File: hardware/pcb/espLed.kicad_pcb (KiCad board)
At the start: 2 copper layers, 23 parts, among them J1 led_strip, J2 flashing, J3 power, Q1 IRF9310TRPBF, Q2 AO3400A, Q3 AO3400A, Q4 AO3400A, SW1 reset, SW2 flash, U1 AMS1117-3.3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

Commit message: connect GNDs of two transistors and make strip's 12v trace thicker
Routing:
- net GND: track 124.1 -> 186.6 mm
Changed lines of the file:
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@@
     (thickness 1.6)
     (drawings 0)
-    (tracks 175)
+    (tracks 191)
     (zones 0)
     (modules 23)
@@
   )
   (setup
-    (last_trace_width 0.6)
+    (last_trace_width 0.4)
     (user_trace_width 0.4)
     (user_trace_width 0.6)
+    (user_trace_width 0.8)
     (trace_clearance 0.3)
     (zone_clearance 0.508)
@@
   (segment (start 182.555 111.252) (end 191.262 111.252) (width 0.4) (layer B.Cu) (net 1))
   (segment (start 176.262 117.545) (end 182.555 111.252) (width 0.4) (layer B.Cu) (net 1))
-  (segment (start 190.246 116.586) (end 191.262 117.602) (width 0.4) (layer F.Cu) (net 1))
-  (segment (start 184.658 117.475) (end 185.547 116.586) (width 0.4) (layer F.Cu) (net 1))
-  (segment (start 184.658 131.064) (end 184.658 117.475) (width 0.4) (layer F.Cu) (net 1))
-  (segment (start 185.814 132.22) (end 184.658 131.064) (width 0.4) (layer F.Cu) (net 1))
-  (segment (start 186.28 132.22) (end 185.814 132.22) (width 0.4) (layer F.Cu) (net 1))
   (segment (start 184.702001 136.906) (end 169.2425 136.906) (width 0.4) (layer F.Cu) (net 1))
   (segment (start 169.2425 136.906) (end 168.148 135.8115) (width 0.4) (layer F.Cu) (net 1))
   (segment (start 186.28 135.328001) (end 184.702001 136.906) (width 0.4) (layer F.Cu) (net 1))
-  (segment (start 192.024 117.602) (end 191.262 117.602) (width 0.4) (layer B.Cu) (net 1))
-  (segment (start 193.04 140.208) (end 193.04 118.618) (width 0.4) (layer B.Cu) (net 1))
+  (segment (start 192.532 117.602) (end 191.262 117.602) (width 0.4) (layer B.Cu) (net 1))
+  (segment (start 193.04 118.11) (end 192.532 117.602) (width 0.4) (layer B.Cu) (net 1))
+  (segment (start 193.04 140.208) (end 193.04 118.11) (width 0.4) (layer B.Cu) (net 1))
   (segment (start 192.278 140.97) (end 193.04 140.208) (width 0.4) (layer B.Cu) (net 1))
-  (segment (start 193.04 118.618) (end 192.024 117.602) (width 0.4) (layer B.Cu) (net 1))
   (segment (start 188.976 140.97) (end 192.278 140.97) (width 0.4) (layer B.Cu) (net 1))
   (segment (start 188.468 140.462) (end 188.976 140.97) (width 0.4) (layer B.Cu) (net 1))
   (segment (start 188.468 138.938) (end 188.468 140.462) (width 0.4) (layer B.Cu) (net 1))
-  (segment (start 191.262 111.252) (end 185.928 116.586) (width 0.4) (layer F.Cu) (net 1))
-  (segment (start 185.928 116.586) (end 190.246 116.586) (width 0.4) (layer F.Cu) (net 1))
-  (segment (start 185.547 116.586) (end 185.928 116.586) (width 0.4) (layer F.Cu) (net 1))
+  (segment (start 187.198 120.65) (end 190.246 117.602) (width 0.8) (layer B.Cu) (net 1))
+  (segment (start 187.198 127.508) (end 187.198 120.65) (width 0.8) (layer B.Cu) (net 1))
+  (segment (start 190.246 117.602) (end 191.262 117.602) (width 0.6) (layer B.Cu) (net 1))
+  (segment (start 182.438 133.366) (end 182.438 132.268) (width 0.6) (layer B.Cu) (net 1))
+  (segment (start 185.293 129.413) (end 187.198 127.508) (width 0.8) (layer B.Cu) (net 1))
+  (segment (start 182.438 132.268) (end 185.293 129.413) (width 0.6) (layer B.Cu) (net 1))
+  (segment (start 173.99 130.048) (end 184.658 130.048) (width 0.6) (layer B.Cu) (net 1))
+  (segment (start 170.942 127) (end 173.99 130.048) (width 0.6) (layer B.Cu) (net 1))
+  (segment (start 164.846 127) (end 170.942 127) (width 0.6) (layer B.Cu) (net 1))
+  (segment (start 184.658 130.048) (end 185.293 129.413) (width 0.8) (layer B.Cu) (net 1))
+  (segment (start 163.068 128.778) (end 164.846 127) (width 0.6) (layer B.Cu) (net 1))
+  (segment (start 163.068 133.096) (end 163.068 128.778) (width 0.6) (layer B.Cu) (net 1))
+  (segment (start 165.862 135.89) (end 163.068 133.096) (width 0.6) (layer B.Cu) (net 1))
+  (segment (start 169.926 135.89) (end 165.862 135.89) (width 0.6) (layer B.Cu) (net 1))
+  (segment (start 172.45 133.366) (end 169.926 135.89) (width 0.6) (layer B.Cu) (net 1))
+  (segment (start 174.818 133.366) (end 172.45 133.366) (width 0.6) (layer B.Cu) (net 1))
+  (segment (start 190.246 117.602) (end 191.262 117.602) (width 0.8) (layer F.Cu) (net 1))
+  (segment (start 189.23 112.081919) (end 189.23 116.586) (width 0.8) (layer F.Cu) (net 1))
+  (segment (start 189.23 116.586) (end 190.246 117.602) (width 0.8) (layer F.Cu) (net 1))
+  (segment (start 190.059919 111.252) (end 189.23 112.081919) (width 0.8) (layer F.Cu) (net 1))
+  (segment (start 191.262 111.252) (end 190.059919 111.252) (width 0.8) (layer F.Cu) (net 1))
+  (segment (start 184.658 131.064) (end 184.658 117.348) (width 0.4) (layer F.Cu) (net 1))
+  (segment (start 185.814 132.22) (end 184.658 131.064) (width 0.4) (layer F.Cu) (net 1))
+  (segment (start 186.28 132.22) (end 185.814 132.22) (width 0.4) (layer F.Cu) (net 1))
+  (segment (start 185.42 116.586) (end 189.23 116.586) (width 0.4) (layer F.Cu) (net 1))
+  (segment (start 184.658 117.348) (end 185.42 116.586) (width 0.4) (layer F.Cu) (net 1))
   (segment (start 176.462 123.7) (end 176.512 123.65) (width 0.4) (layer B.Cu) (net 2))
   (segment (start 174.0995 123.7) (end 176.462 123.7) (width 0.4) (layer B.Cu) (net 2))
@@
   (segment (start 183.642 113.792) (end 181.562 115.872) (width 0.4) (layer B.Cu) (net 9))
   (segment (start 191.262 113.792) (end 183.642 113.792) (width 0.4) (layer B.Cu) (net 9))
-  (segment (start 175.514 141.732) (end 174.498 140.716) (width 0.6) (layer B.Cu) (net 9))
-  (segment (start 187.99801 141.77001) (end 187.96 141.732) (width 0.6) (layer B.Cu) (net 9))
-  (segment (start 192.805682 141.77001) (end 187.99801 141.77001) (width 0.6) (layer B.Cu) (net 9))
-  (segment (start 194.818 139.757692) (end 192.805682 141.77001) (width 0.6) (layer B.Cu) (net 9))
-  (segment (start 194.818 115.316) (end 194.818 139.757692) (width 0.6) (layer B.Cu) (net 9))
-  (segment (start 187.96 141.732) (end 175.514 141.732) (width 0.6) (layer B.Cu) (net 9))
-  (segment (start 193.294 113.792) (end 194.818 115.316) (width 0.6) (layer B.Cu) (net 9))
-  (segment (start 174.498 140.716) (end 174.498 138.938) (width 0.6) (layer B.Cu) (net 9))
-  (segment (start 191.262 113.792) (end 193.294 113.792) (width 0.6) (layer B.Cu) (net 9))
+  (segment (start 174.498 140.716) (end 174.498 138.938) (width 0.8) (layer B.Cu) (net 9))
+  (segment (start 175.768 141.986) (end 174.498 140.716) (width 0.8) (layer B.Cu) (net 9))
+  (segment (start 193.04 141.986) (end 175.768 141.986) (width 0.8) (layer B.Cu) (net 9))
+  (segment (start 194.056 140.97) (end 193.04 141.986) (width 0.8) (layer B.Cu) (net 9))
+  (segment (start 194.056 114.554) (end 194.056 140.97) (width 0.8) (layer B.Cu) (net 9))
+  (segment (start 193.294 113.792) (end 194.056 114.554) (width 0.8) (layer B.Cu) (net 9))
+  (segment (start 191.262 113.792) (end 193.294 113.792) (width 0.8) (layer B.Cu) (net 9))
   (via (at 191.008 126.492) (size 1.6) (drill 1) (layers F.Cu B.Cu) (net 10))
   (segment (start 192.1995 127.6835) (end 191.008 126.492) (width 0.4) (layer F.Cu) (net 10))

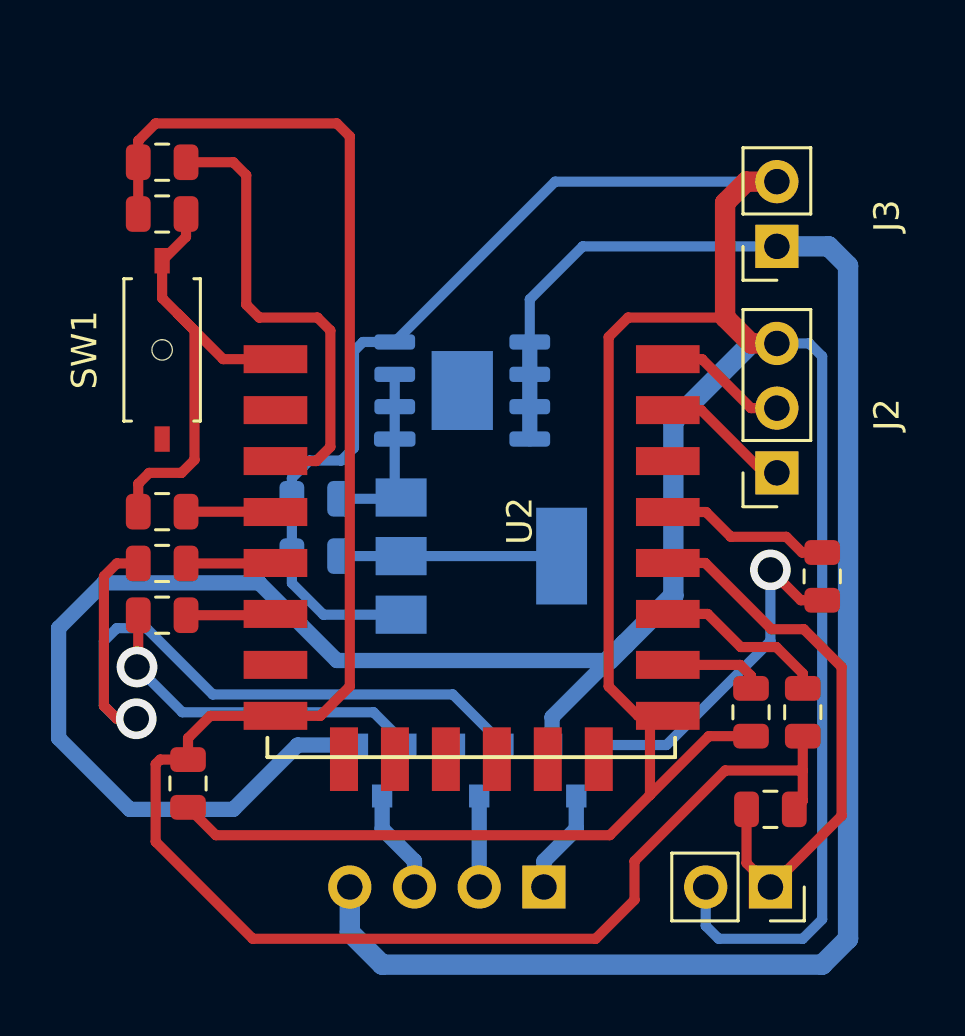
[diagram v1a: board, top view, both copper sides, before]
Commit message: connect GND of the remaining transistor and make 12V traces thicker
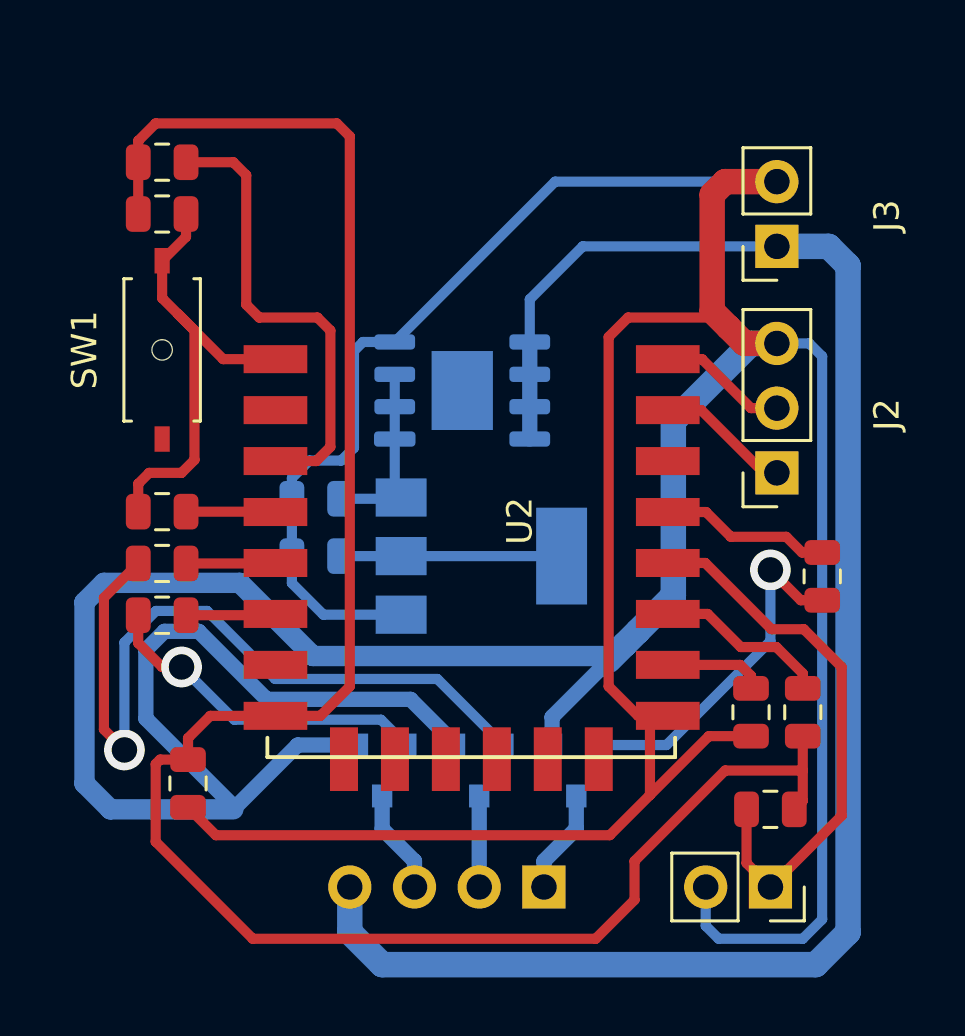
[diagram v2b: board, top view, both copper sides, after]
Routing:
- net GND: track 186.6 -> 211.5 mm
- net Net-(Q4-Pad2): track 13.9 -> 13.3 mm

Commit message: connect 3v3 of the regulator to ESP and connect GND of the "reset" btn
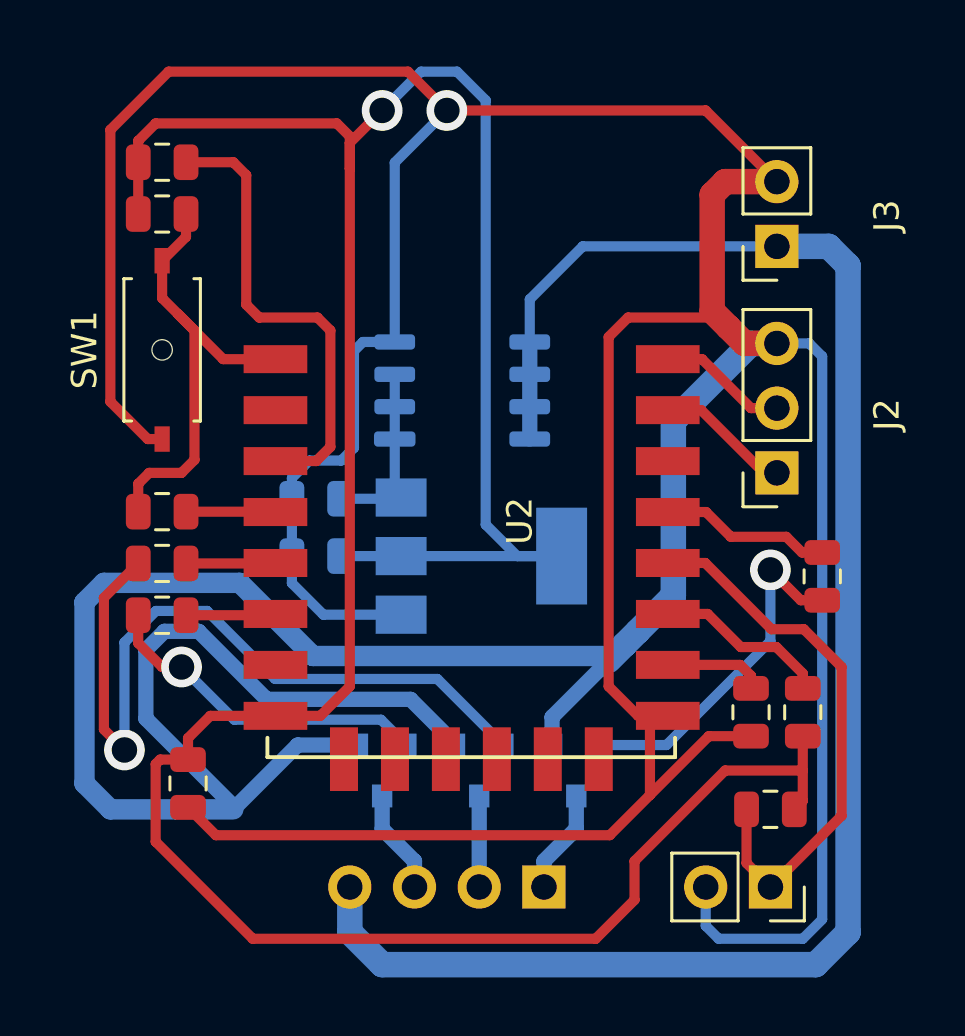
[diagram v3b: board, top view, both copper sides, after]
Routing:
- net GND: track 211.5 -> 246.0 mm, vias 0 -> 1
- net +3V3: track 88.6 -> 116.7 mm, vias 0 -> 1
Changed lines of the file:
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@@
     (thickness 1.6)
     (drawings 0)
-    (tracks 202)
+    (tracks 221)
     (zones 0)
     (modules 23)
@@
     (fp_line (start 3.7 -2.7) (end 3.7 2.7) (layer B.CrtYd) (width 0.05))
     (fp_line (start 3.7 2.7) (end -3.7 2.7) (layer B.CrtYd) (width 0.05))
-    (fp_text user %R (at 0 0 180) (layer B.Fab)
-      (effects (font (size 0.98 0.98) (thickness 0.15)) (justify mirror))
-    )
     (pad 3 smd roundrect (at -2.65 1.905) (size 1.63 0.6) (layers B.Cu B.Paste B.Mask) (roundrect_rratio 0.25)
       (net 2 +12V))
@@
     (pad 1 smd roundrect (at 2.65 1.905) (size 1.6 0.6) (layers B.Cu B.Paste B.Mask) (roundrect_rratio 0.25)
       (net 9 /12v_in))
-    (pad 9 smd rect (at 0 0) (size 2.41 3.1) (layers B.Cu B.Mask))
-    (pad "" smd roundrect (at -0.6 0.775) (size 0.97 1.25) (layers B.Paste) (roundrect_rratio 0.25))
-    (pad "" smd roundrect (at -0.6 -0.775) (size 0.97 1.25) (layers B.Paste) (roundrect_rratio 0.25))
-    (pad "" smd roundrect (at 0.6 0.775) (size 0.97 1.25) (layers B.Paste) (roundrect_rratio 0.25))
-    (pad "" smd roundrect (at 0.6 -0.775) (size 0.97 1.25) (layers B.Paste) (roundrect_rratio 0.25))
     (model ${KISYS3DMOD}/Package_SO.3dshapes/HSOP-8-1EP_3.9x4.9mm_P1.27mm_EP2.41x3.1mm.wrl
       (at (xyz 0 0 0))
@@
   (segment (start 188.590501 133.0175) (end 186.28 135.328001) (width 0.4) (layer F.Cu) (net 1))
   (segment (start 190.246 133.0175) (end 188.590501 133.0175) (width 0.4) (layer F.Cu) (net 1))
-  (segment (start 182.555 111.252) (end 191.262 111.252) (width 0.4) (layer B.Cu) (net 1))
-  (segment (start 176.262 117.545) (end 182.555 111.252) (width 0.4) (layer B.Cu) (net 1))
   (segment (start 184.702001 136.906) (end 169.2425 136.906) (width 0.4) (layer F.Cu) (net 1))
   (segment (start 169.2425 136.906) (end 168.148 135.8115) (width 0.4) (layer F.Cu) (net 1))
@@
   (segment (start 189.357 116.967) (end 188.722 116.332) (width 1) (layer F.Cu) (net 1))
   (segment (start 189.992 117.602) (end 189.357 116.967) (width 1) (layer F.Cu) (net 1))
+  (via (at 178.308 108.458) (size 1.6) (drill 1) (layers F.Cu B.Cu) (net 1))
+  (segment (start 176.262 117.545) (end 176.262 110.504) (width 0.4) (layer B.Cu) (net 1))
+  (segment (start 176.262 110.504) (end 178.308 108.458) (width 0.4) (layer B.Cu) (net 1))
+  (segment (start 191.262 111.252) (end 188.468 108.458) (width 0.4) (layer F.Cu) (net 1))
+  (segment (start 188.468 108.458) (end 178.308 108.458) (width 0.4) (layer F.Cu) (net 1))
+  (segment (start 166.568 121.356) (end 167.132 121.356) (width 0.4) (layer F.Cu) (net 1))
+  (segment (start 165.1 119.888) (end 166.568 121.356) (width 0.4) (layer F.Cu) (net 1))
+  (segment (start 165.1 109.22) (end 165.1 119.888) (width 0.4) (layer F.Cu) (net 1))
+  (segment (start 167.386 106.934) (end 165.1 109.22) (width 0.4) (layer F.Cu) (net 1))
+  (segment (start 176.784 106.934) (end 167.386 106.934) (width 0.4) (layer F.Cu) (net 1))
+  (segment (start 178.308 108.458) (end 176.784 106.934) (width 0.4) (layer F.Cu) (net 1))
   (segment (start 176.462 123.7) (end 176.512 123.65) (width 0.4) (layer B.Cu) (net 2))
   (segment (start 174.0995 123.7) (end 176.462 123.7) (width 0.4) (layer B.Cu) (net 2))
@@
   (segment (start 166.878 134.112) (end 167.0535 133.9365) (width 0.4) (layer F.Cu) (net 3))
   (segment (start 173.342 132.22) (end 172.28 132.22) (width 0.4) (layer F.Cu) (net 3))
-  (segment (start 174.498 109.474) (end 174.498 131.064) (width 0.4) (layer F.Cu) (net 3))
   (segment (start 173.99 108.966) (end 174.498 109.474) (width 0.4) (layer F.Cu) (net 3))
   (segment (start 174.498 131.064) (end 173.342 132.22) (width 0.4) (layer F.Cu) (net 3))
@@
   (segment (start 166.1945 109.6495) (end 166.878 108.966) (width 0.4) (layer F.Cu) (net 3))
   (segment (start 166.1945 110.49) (end 166.1945 109.6495) (width 0.4) (layer F.Cu) (net 3))
+  (segment (start 182.812 125.95) (end 181.068 125.95) (width 0.4) (layer B.Cu) (net 3))
+  (segment (start 181.068 125.95) (end 179.832 124.714) (width 0.4) (layer B.Cu) (net 3))
+  (segment (start 179.832 108.057998) (end 178.708002 106.934) (width 0.4) (layer B.Cu) (net 3))
+  (segment (start 179.832 124.714) (end 179.832 108.057998) (width 0.4) (layer B.Cu) (net 3))
+  (via (at 175.768 108.458) (size 1.6) (drill 1) (layers F.Cu B.Cu) (net 3))
+  (segment (start 177.292 106.934) (end 175.768 108.458) (width 0.4) (layer B.Cu) (net 3))
+  (segment (start 178.708002 106.934) (end 177.292 106.934) (width 0.4) (layer B.Cu) (net 3))
+  (segment (start 174.498 109.728) (end 174.498 110.744) (width 0.4) (layer F.Cu) (net 3))
+  (segment (start 175.768 108.458) (end 174.498 109.728) (width 0.4) (layer F.Cu) (net 3))
+  (segment (start 174.498 110.744) (end 174.498 131.064) (width 0.4) (layer F.Cu) (net 3))
+  (segment (start 174.498 109.474) (end 174.498 110.744) (width 0.4) (layer F.Cu) (net 3))
   (segment (start 175.768 136.652) (end 177.038 137.922) (width 0.6) (layer B.Cu) (net 4))
   (segment (start 177.038 137.922) (end 177.038 138.938) (width 0.6) (layer B.Cu) (net 4))
@@
   (segment (start 186.28 120.22) (end 188.292 120.22) (width 0.4) (layer F.Cu) (net 8))
   (segment (start 181.562 117.545) (end 181.562 121.355) (width 0.6) (layer B.Cu) (net 9))
-  (segment (start 181.562 115.872) (end 181.562 117.545) (width 0.4) (layer B.Cu) (net 9))
-  (segment (start 183.642 113.792) (end 181.562 115.872) (width 0.4) (layer B.Cu) (net 9))
-  (segment (start 191.262 113.792) (end 183.642 113.792) (width 0.4) (layer B.Cu) (net 9))
   (segment (start 175.768 141.986) (end 174.498 140.716) (width 1) (layer B.Cu) (net 9))
   (segment (start 192.786 141.986) (end 175.768 141.986) (width 1) (layer B.Cu) (net 9))
@@
   (segment (start 193.294 113.792) (end 194.056 114.554) (width 1) (layer B.Cu) (net 9))
   (segment (start 191.262 113.792) (end 193.294 113.792) (width 1) (layer B.Cu) (net 9))
+  (segment (start 181.562 115.872) (end 181.562 117.545) (width 0.4) (layer B.Cu) (net 9))
+  (segment (start 183.642 113.792) (end 181.562 115.872) (width 0.4) (layer B.Cu) (net 9))
+  (segment (start 191.262 113.792) (end 183.642 113.792) (width 0.4) (layer B.Cu) (net 9))
   (via (at 191.008 126.492) (size 1.6) (drill 1) (layers F.Cu B.Cu) (net 10))
   (segment (start 192.1995 127.6835) (end 191.008 126.492) (width 0.4) (layer F.Cu) (net 10))
